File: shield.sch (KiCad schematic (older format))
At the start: 2 parts

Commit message: add CAN interfaces with connectors
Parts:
- added CONN?: I2C, MODULE, symbol I2C
- added CONN?: SPI, symbol SPI
- added CONN?: UART, MODULE, symbol UART
- added CONN?: SERVO, symbol SERVO
- added P?: CONN_02X04, symbol CONN_02X04
- added P?: Servo_5V, symbol CONN_01X02
- added P?: CAN_5V, symbol CONN_01X02
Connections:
- net labels added: GND, GPIO1, GPIO2, GPIO3, GPIO4
- wire segments 0 -> 1
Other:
- moved on the sheet: U?A, U?B
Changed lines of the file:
@@
 $Descr A4 11693 8268
 encoding utf-8
-Sheet 1 1
+Sheet 1 2
 Title "CVRA Nucleo144 shield"
 Date "2016-09-19"
@@
 L ST_Nucleo144_F429ZI_Morpho U?
 U 1 1 57E0016C
-P 3500 3750
-F 0 "U?" H 3250 5600 60  0000 C CNN
-F 1 "ST_Nucleo144_F429ZI_Morpho" V 3500 3750 60  0000 C CNN
-F 2 "" H 3500 4100 60  0000 C CNN
-F 3 "" H 3500 4100 60  0000 C CNN
-	1    3500 3750
+P 2050 2850
+F 0 "U?" H 1800 4700 60  0000 C CNN
+F 1 "ST_Nucleo144_F429ZI_Morpho" V 2050 2850 60  0000 C CNN
+F 2 "" H 2050 3200 60  0000 C CNN
+F 3 "" H 2050 3200 60  0000 C CNN
+	1    2050 2850
 	1    0    0    -1
 $EndComp
@@
 L ST_Nucleo144_F429ZI_Morpho U?
 U 2 1 57E00191
-P 6000 3750
-F 0 "U?" H 5750 5600 60  0000 C CNN
-F 1 "ST_Nucleo144_F429ZI_Morpho" V 6000 3750 60  0000 C CNN
-F 2 "" H 6000 4100 60  0000 C CNN
-F 3 "" H 6000 4100 60  0000 C CNN
-	2    6000 3750
+P 4150 2850
+F 0 "U?" H 3900 4700 60  0000 C CNN
+F 1 "ST_Nucleo144_F429ZI_Morpho" V 4150 2850 60  0000 C CNN
+F 2 "" H 4150 3200 60  0000 C CNN
+F 3 "" H 4150 3200 60  0000 C CNN
+	2    4150 2850
 	1    0    0    -1
 $EndComp
@@
 	1    0    0    -1
 $EndComp
+$Comp
+L I2C CONN?
+U 1 1 5817142A
+P 6700 4400
+F 0 "CONN?" H 6700 4750 50  0000 C CNN
+F 1 "I2C" H 6700 4050 50  0000 C CNN
+F 2 "MODULE" H 6700 4400 50  0001 C CNN
+F 3 "DOCUMENTATION" H 6700 4400 50  0001 C CNN
+	1    6700 4400
+	1    0    0    -1
+$EndComp
+$Comp
+L SPI CONN?
+U 1 1 5817144F
+P 7100 5600
+F 0 "CONN?" H 6700 6300 50  0000 C CNN
+F 1 "SPI" H 6700 5400 50  0000 C CNN
+F 2 "" H 7000 6150 39  0000 C CNN
+F 3 "" H 7000 6150 39  0000 C CNN
+	1    7100 5600
+	1    0    0    -1
+$EndComp
+$Comp
+L UART CONN?
+U 1 1 58171483
+P 6700 3450
+F 0 "CONN?" H 6700 3800 50  0000 C CNN
+F 1 "UART" H 6700 3100 50  0000 C CNN
+F 2 "MODULE" H 6700 3450 50  0001 C CNN
+F 3 "DOCUMENTATION" H 6700 3450 50  0001 C CNN
+	1    6700 3450
+	1    0    0    -1
+$EndComp
+$Comp
+L CONN_02X04 P?
+U 1 1 58171A60
+P 9150 4800
+F 0 "P?" H 9150 5050 50  0000 C CNN
+F 1 "CONN_02X04" H 9150 4550 50  0000 C CNN
+F 2 "" H 9150 3600 50  0000 C CNN
+F 3 "" H 9150 3600 50  0000 C CNN
+	1    9150 4800
+	1    0    0    -1
+$EndComp
+$Comp
+L GND #PWR?
+U 1 1 58171B98
+P 9400 5000
+F 0 "#PWR?" H 9400 5000 30  0001 C CNN
+F 1 "GND" H 9400 4930 30  0001 C CNN
+F 2 "" H 9400 5000 60  0000 C CNN
+F 3 "" H 9400 5000 60  0000 C CNN
+	1    9400 5000
+	1    0    0    -1
+$EndComp
+Text Label 8900 4650 2    50   ~ 0
+GPIO1
+Text Label 8900 4750 2    50   ~ 0
+GPIO2
+Text Label 8900 4850 2    50   ~ 0
+GPIO3
+Text Label 8900 4950 2    50   ~ 0
+GPIO4
+Wire Wire Line
+	9400 4650 9400 5000
+Connection ~ 9400 4750
+Connection ~ 9400 4850
+Connection ~ 9400 4950
+$Sheet
+S 9350 800  1550 1000
+U 58172972
+F0 "CAN interfaces" 60
+F1 "can_interfaces.sch" 60
+F2 "CAN1_RX" I L 9350 900 60
+F3 "CAN1_TX" O L 9350 1000 60
+F4 "CAN2_RX" I L 9350 1200 60
+F5 "CAN2_TX" O L 9350 1300 60
+$EndSheet
+$Comp
+L CONN_01X02 P?
+U 1 1 58173DDD
+P 6650 1000
+F 0 "P?" H 6650 1150 50  0000 C CNN
+F 1 "Servo_5V" V 6750 1000 50  0000 C CNN
+F 2 "" H 6650 1000 50  0000 C CNN
+F 3 "" H 6650 1000 50  0000 C CNN
+	1    6650 1000
+	1    0    0    -1
+$EndComp
+$Comp
+L CONN_01X02 P?
+U 1 1 58173F03
+P 6650 1400
+F 0 "P?" H 6650 1550 50  0000 C CNN
+F 1 "CAN_5V" V 6750 1400 50  0000 C CNN
+F 2 "" H 6650 1400 50  0000 C CNN
+F 3 "" H 6650 1400 50  0000 C CNN
+	1    6650 1400
+	1    0    0    -1
+$EndComp
+$Comp
+L SERVO CONN?
+U 1 1 58176E5D
+P 5650 6750
+F 0 "CONN?" H 5650 7000 60  0000 C CNN
+F 1 "SERVO" H 5650 6500 60  0000 C CNN
+F 2 "" H 5650 6750 60  0000 C CNN
+F 3 "" H 5650 6750 60  0000 C CNN
+	1    5650 6750
+	1    0    0    -1
+$EndComp

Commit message: SD card
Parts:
- added C? (x2): C, symbol C
- added CONN?: MICRO_SD, MODULE, symbol MICRO_SD
- added Q?: Q_PMOS_DGS, symbol Q_PMOS_DGS
- added R?: R, symbol R
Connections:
- net labels added: SDIO_CK, SDIO_CMD, SDIO_D0, SDIO_D1, SDIO_D2, SDIO_D3, SD_DETECT, SD_PWR, VCC
- wire segments 1 -> 21
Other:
- moved on the sheet: U?B
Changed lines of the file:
@@
 L ST_Nucleo144_F429ZI_Morpho U?
 U 2 1 57E00191
-P 4150 2850
-F 0 "U?" H 3900 4700 60  0000 C CNN
-F 1 "ST_Nucleo144_F429ZI_Morpho" V 4150 2850 60  0000 C CNN
-F 2 "" H 4150 3200 60  0000 C CNN
-F 3 "" H 4150 3200 60  0000 C CNN
-	2    4150 2850
+P 4450 2850
+F 0 "U?" H 4200 4700 60  0000 C CNN
+F 1 "ST_Nucleo144_F429ZI_Morpho" V 4450 2850 60  0000 C CNN
+F 2 "" H 4450 3200 60  0000 C CNN
+F 3 "" H 4450 3200 60  0000 C CNN
+	2    4450 2850
 	1    0    0    -1
 $EndComp
@@
 Text Label 8900 4950 2    50   ~ 0
 GPIO4
-Wire Wire Line
-	9400 4650 9400 5000
-Connection ~ 9400 4750
-Connection ~ 9400 4850
-Connection ~ 9400 4950
 $Sheet
 S 9350 800  1550 1000
@@
 	1    0    0    -1
 $EndComp
+$Comp
+L MICRO_SD CONN?
+U 1 1 581F8DEC
+P 2400 7000
+F 0 "CONN?" H 2600 7500 50  0000 C CNN
+F 1 "MICRO_SD" H 2200 7500 50  0000 C CNN
+F 2 "MODULE" H 2500 7000 50  0001 C CNN
+F 3 "DOCUMENTATION" H 2500 7000 50  0001 C CNN
+	1    2400 7000
+	1    0    0    -1
+$EndComp
+Text Label 1800 7250 2    50   ~ 0
+SDIO_D0
+Text Label 1800 7350 2    50   ~ 0
+SDIO_D1
+Text Label 1800 6650 2    50   ~ 0
+SDIO_D2
+Text Label 1800 6750 2    50   ~ 0
+SDIO_D3
+Text Label 1800 6850 2    50   ~ 0
+SDIO_CMD
+Text Label 1800 7050 2    50   ~ 0
+SDIO_CK
+Text Label 5800 1550 2    50   ~ 0
+SD_DETECT
+Text Label 1900 7650 0    50   ~ 0
+SD_DETECT
+Text Label 1400 1250 2    50   ~ 0
+SDIO_CK
+Text Label 2700 1150 0    50   ~ 0
+SDIO_D3
+Text Label 1400 1150 2    50   ~ 0
+SDIO_D2
+Text Label 3800 1150 2    50   ~ 0
+SDIO_D1
+Text Label 5100 1150 0    50   ~ 0
+SDIO_D0
+Text Label 2700 1250 0    50   ~ 0
+SDIO_CMD
+$Comp
+L GND #PWR?
+U 1 1 581FB6B3
+P 2650 7600
+F 0 "#PWR?" H 2650 7600 30  0001 C CNN
+F 1 "GND" H 2650 7530 30  0001 C CNN
+F 2 "" H 2650 7600 60  0000 C CNN
+F 3 "" H 2650 7600 60  0000 C CNN
+	1    2650 7600
+	1    0    0    -1
+$EndComp
+Text Label 600  6450 0    50   ~ 0
+SD_PWR
+$Comp
+L C C?
+U 1 1 581FBF5C
+P 1200 7000
+F 0 "C?" H 1225 7100 50  0000 L CNN
+F 1 "C" H 1225 6900 50  0000 L CNN
+F 2 "" H 1238 6850 50  0000 C CNN
+F 3 "" H 1200 7000 50  0000 C CNN
+	1    1200 7000
+	1    0    0    -1
+$EndComp
+$Comp
+L C C?
+U 1 1 581FC04F
+P 1000 7000
+F 0 "C?" H 1025 7100 50  0000 L CNN
+F 1 "C" H 1025 6900 50  0000 L CNN
+F 2 "" H 1038 6850 50  0000 C CNN
+F 3 "" H 1000 7000 50  0000 C CNN
+	1    1000 7000
+	1    0    0    -1
+$EndComp
+$Comp
+L VCC #PWR?
+U 1 1 581FC17F
+P 1200 6200
+F 0 "#PWR?" H 1200 6300 30  0001 C CNN
+F 1 "VCC" H 1200 6300 30  0000 C CNN
+F 2 "" H 1200 6200 60  0000 C CNN
+F 3 "" H 1200 6200 60  0000 C CNN
+	1    1200 6200
+	1    0    0    -1
+$EndComp
+$Comp
+L GND #PWR?
+U 1 1 581FC1DB
+P 1200 7200
+F 0 "#PWR?" H 1200 7200 30  0001 C CNN
+F 1 "GND" H 1200 7130 30  0001 C CNN
+F 2 "" H 1200 7200 60  0000 C CNN
+F 3 "" H 1200 7200 60  0000 C CNN
+	1    1200 7200
+	1    0    0    -1
+$EndComp
+Wire Wire Line
+	9400 4650 9400 4750
+Wire Wire Line
+	9400 4750 9400 4850
+Wire Wire Line
+	9400 4850 9400 4950
+Wire Wire Line
+	9400 4950 9400 5000
+Connection ~ 9400 4750
+Connection ~ 9400 4850
+Connection ~ 9400 4950
+Wire Wire Line
+	2350 7550 2350 7650
+Wire Wire Line
+	2350 7650 1900 7650
+Wire Wire Line
+	2450 7550 2650 7550
+Wire Wire Line
+	2650 7550 2650 7600
+Connection ~ 2650 7550
+Wire Wire Line
+	1000 7150 1200 7150
+Wire Wire Line
+	1200 7150 1800 7150
+Connection ~ 1200 7150
+Wire Wire Line
+	1800 6950 1400 6950
+Wire Wire Line
+	1400 6950 1400 6850
+Wire Wire Line
+	1400 6850 1200 6850
+Wire Wire Line
+	1200 6850 1000 6850
+Connection ~ 1200 6850
+Wire Wire Line
+	1200 7200 1200 7150
+$Comp
+L Q_PMOS_DGS Q?
+U 1 1 581FC8E7
+P 1100 6450
+F 0 "Q?" H 1400 6500 50  0000 R CNN
+F 1 "Q_PMOS_DGS" H 1750 6400 50  0000 R CNN
+F 2 "" H 1300 6550 50  0000 C CNN
+F 3 "" H 1100 6450 50  0000 C CNN
+	1    1100 6450
+	1    0    0    -1
+$EndComp
+Wire Wire Line
+	600  6450 850  6450
+Wire Wire Line
+	850  6450 900  6450
+Wire Wire Line
+	1200 6200 1200 6250
+$Comp
+L R R?
+U 1 1 581FD060
+P 1000 6200
+F 0 "R?" V 1080 6200 50  0000 C CNN
+F 1 "R" V 1000 6200 50  0000 C CNN
+F 2 "" V 930 6200 50  0000 C CNN
+F 3 "" H 1000 6200 50  0000 C CNN
+	1    1000 6200
+	0    1    1    0
+$EndComp
+Wire Wire Line
+	1150 6200 1200 6200
+Connection ~ 1200 6200
+Wire Wire Line
+	850  6200 850  6450
+Connection ~ 850  6450
+Wire Wire Line
+	1200 6650 1200 6850
+Text Label 5450 1300 0    50   ~ 0
+SD_PWR
 $EndSCHEMATC

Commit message: interface panel connector
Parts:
- removed P?: CONN_02X04, symbol CONN_02X04
- added P?: CONN_02X10, symbol CONN_02X10
- added P?: CONN_02X05, symbol CONN_02X05
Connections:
- net labels added: +5V
- wire segments 21 -> 34
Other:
- moved on the sheet: C?, CONN?, P?, Q?, R?

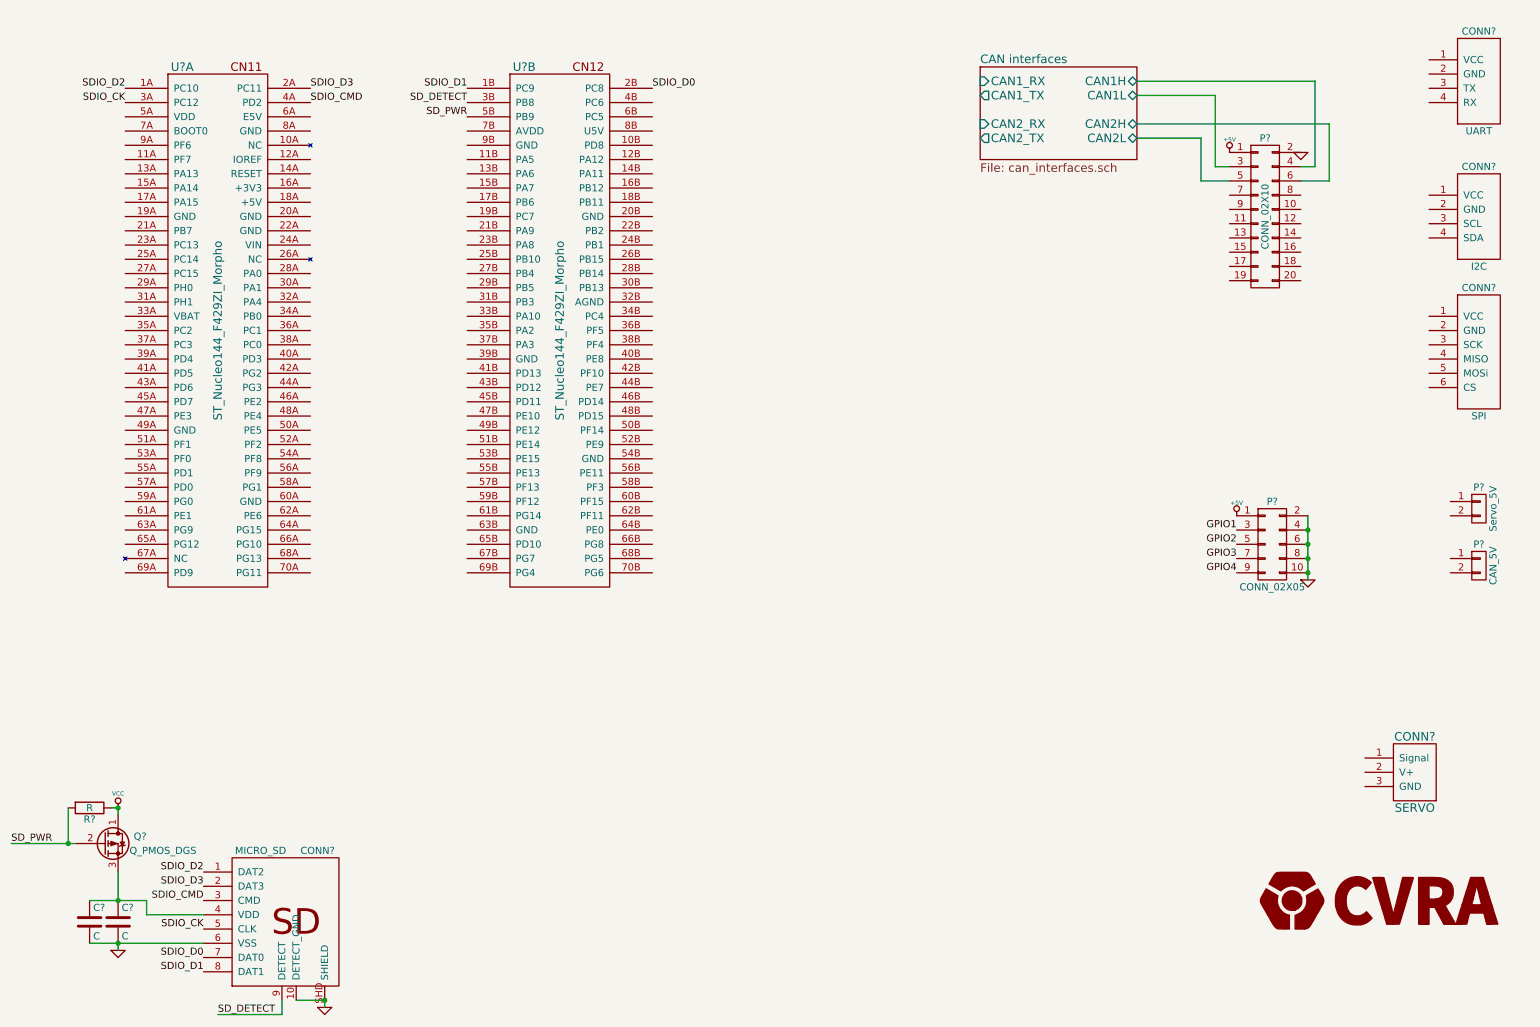
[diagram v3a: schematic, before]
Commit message: gpio assignment, servos PWM chip
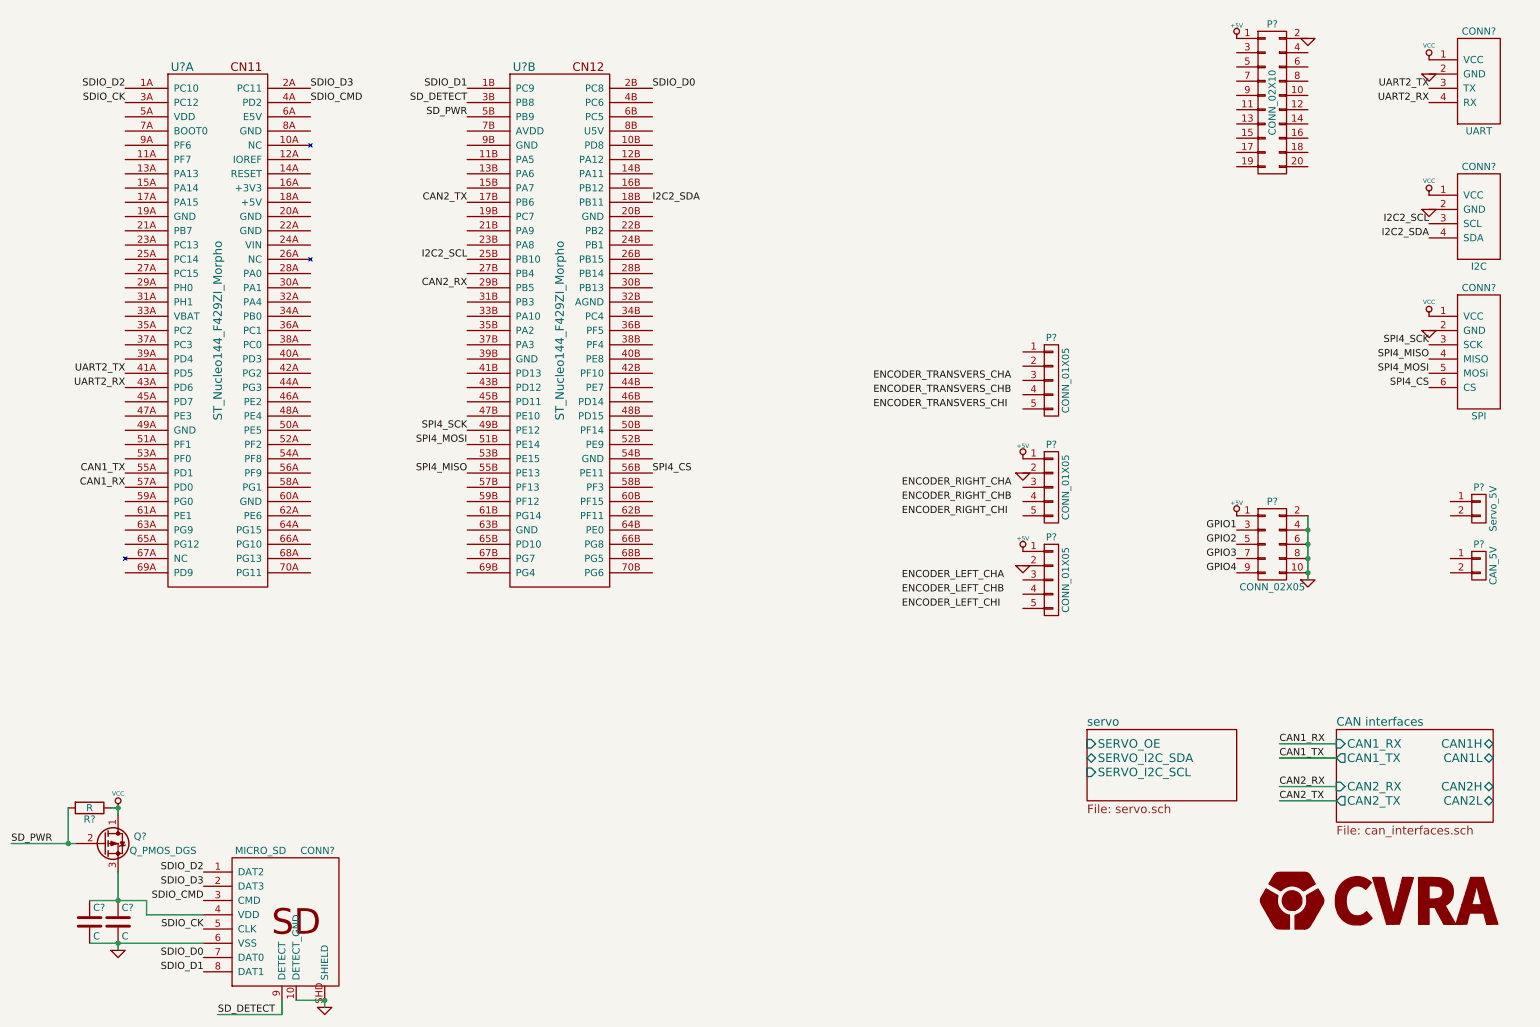
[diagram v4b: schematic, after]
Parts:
- removed CONN?: SERVO, symbol SERVO
- added P? (x3): CONN_01X05, symbol CONN_01X05
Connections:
- net +5V: now also P?.1 (P1), P?.1 (P1)
- net CAN interfaces/CAN1H: no longer P?.4 (P4)
- net CAN interfaces/CAN1L: no longer P?.3 (P3)
- net CAN interfaces/CAN2H: no longer P?.6 (P6)
- net CAN interfaces/CAN2L: no longer P?.5 (P5)
- net GND: now also CONN?.2 (GND), CONN?.2 (GND), CONN?.2 (GND), P?.2 (P2), P?.2 (P2)
- net VCC: now also CONN?.1 (VCC), CONN?.1 (VCC), CONN?.1 (VCC)
- net UART2_TX: now reaches U?.41A (PD5)
- net UART2_TX: now also CONN?.3 (TX)
- net UART2_RX: now reaches U?.43A (PD6)
- net UART2_RX: now also CONN?.4 (RX)
- net CAN1_TX: now reaches U?.55A (PD1)
- net CAN1_RX: now reaches U?.57A (PD0)
- net CAN2_TX: now reaches U?.17B (PB6)
- net I2C2_SDA: now reaches U?.18B (PB11)
- net I2C2_SDA: now also CONN?.4 (SDA)
- net I2C2_SCL: now reaches U?.25B (PB10)
- net I2C2_SCL: now also CONN?.3 (SCL)
- net CAN2_RX: now reaches U?.29B (PB5)
- net SPI4_SCK: now reaches U?.49B (PE12)
- net SPI4_SCK: now also CONN?.3 (SCK)
- net SPI4_MOSI: now reaches U?.51B (PE14)
- net SPI4_MOSI: now also CONN?.5 (MOSi)
- net SPI4_MISO: now reaches U?.55B (PE13)
- net SPI4_MISO: now also CONN?.4 (MISO)
- net SPI4_CS: now reaches U?.56B (PE11)
- net SPI4_CS: now also CONN?.6 (CS)
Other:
- moved on the sheet: P?
